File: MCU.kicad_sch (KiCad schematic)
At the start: 46 parts, among them J1 USB_C_Receptacle_USB2.0_16P, J2 DE9_Pins_MountingHoles, Q1 BC817, Q2 BC817, Q3 BC817, Q4 BC817, SW1 SW_SPST, SW2 SW_SPST, U1 W25Q128JVS, U2 ESP32-S3-MINI-1U, U3 MAX3232

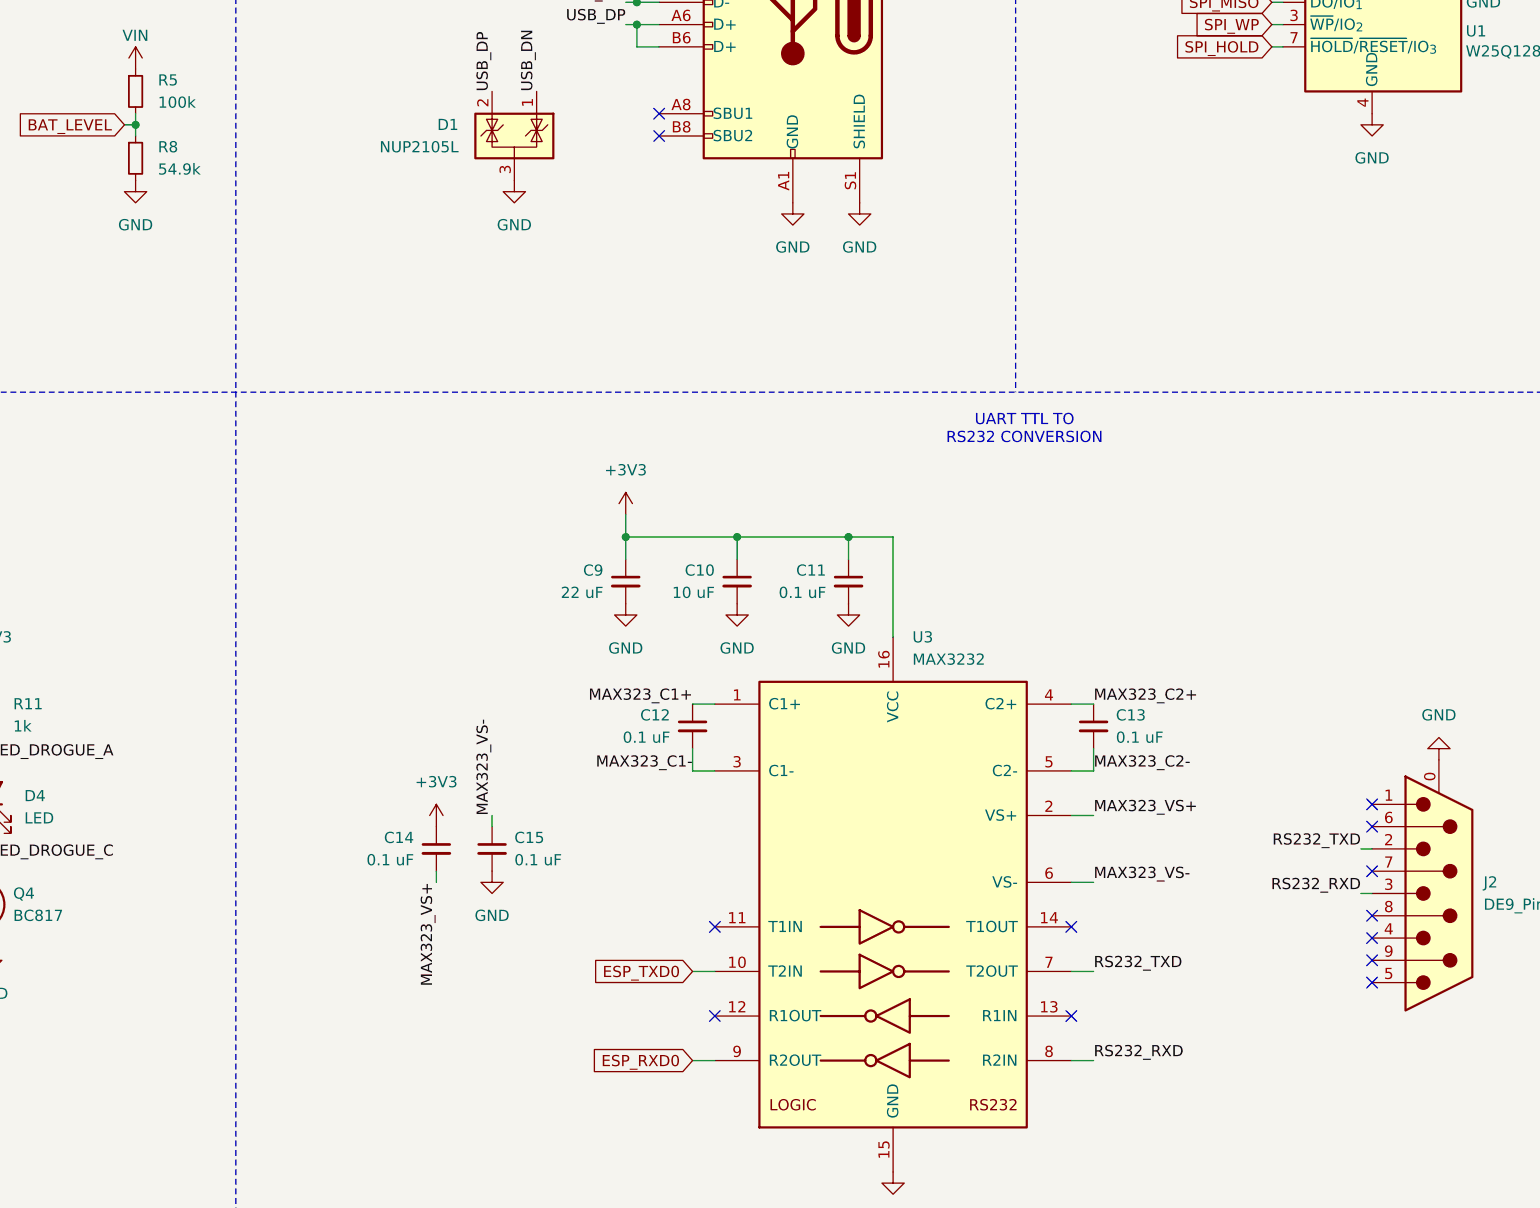
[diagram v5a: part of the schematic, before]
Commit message: updated some values and routed some preliminary roads
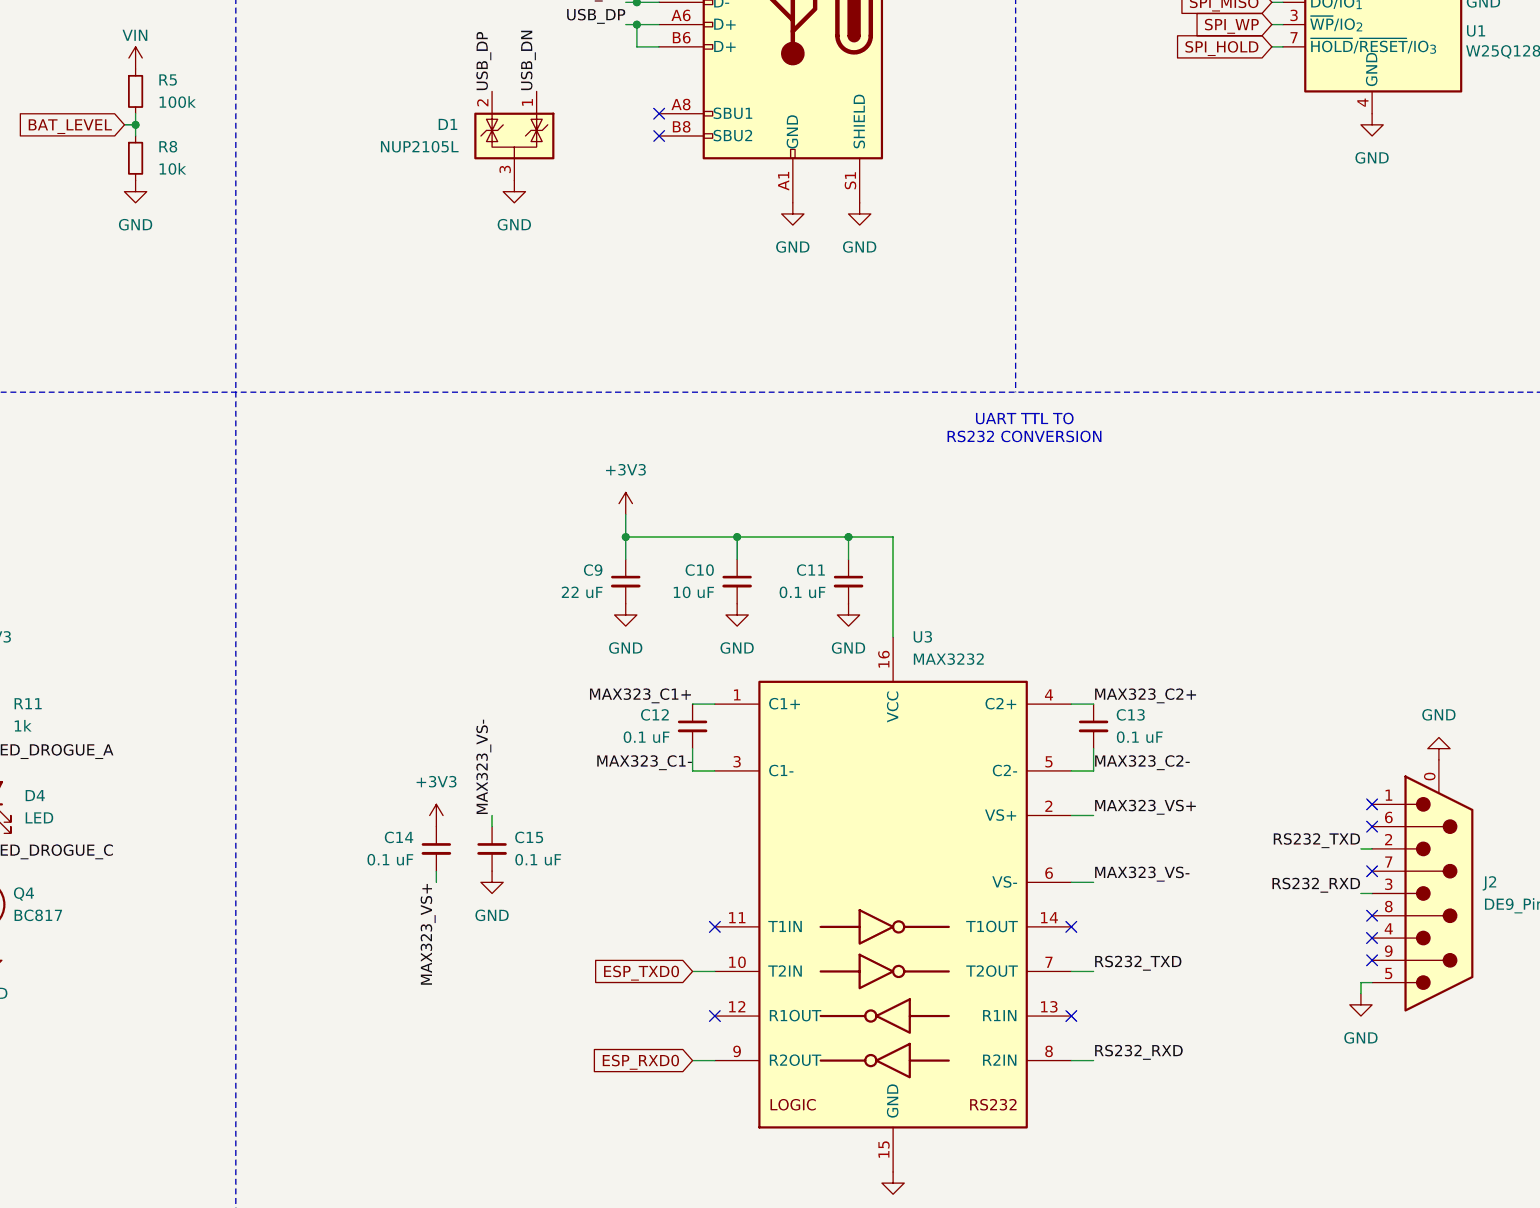
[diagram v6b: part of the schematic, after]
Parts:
- R8: value 54.9k -> 10k
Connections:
- net GND: now also J2.5
- no-connect marks 23 -> 22
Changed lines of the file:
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@@
 	)
 	(no_connect
-		(at 322.58 175.26)
-	)
-	(no_connect
 		(at 102.87 55.88)
 	)
@@
 	(wire
 		(pts
+			(xy 322.58 175.26) (xy 321.31 175.26)
+		)
+		(stroke
+			(width 0)
+			(type default)
+		)
+	)
+	(wire
+		(pts
 			(xy 347.98 57.15) (xy 347.98 58.42)
 		)
@@
 	(wire
 		(pts
+			(xy 321.31 175.26) (xy 321.31 176.53)
+		)
+		(stroke
+			(width 0)
+			(type default)
+		)
+	)
+	(wire
+		(pts
 			(xy 288.29 151.13) (xy 290.83 151.13)
 		)
@@
 	)
 	(symbol
+		(lib_id "power:GND")
+		(at 321.31 176.53 0)
+		(unit 1)
+		(exclude_from_sim no)
+		(in_bom yes)
+		(on_board yes)
+		(dnp no)
+		(fields_autoplaced yes)
+		(property "Reference" "#PWR0119"
+			(at 321.31 182.88 0)
+			(effects
+				(font
+					(size 1.27 1.27)
+				)
+				(hide yes)
+			)
+		)
+		(property "Value" "GND"
+			(at 321.31 181.61 0)
+			(effects
+				(font
+					(size 1.27 1.27)
+				)
+			)
+		)
+		(property "Footprint" ""
+			(at 321.31 176.53 0)
+			(effects
+				(font
+					(size 1.27 1.27)
+				)
+				(hide yes)
+			)
+		)
+		(property "Datasheet" ""
+			(at 321.31 176.53 0)
+			(effects
+				(font
+					(size 1.27 1.27)
+				)
+				(hide yes)
+			)
+		)
+		(property "Description" "Power symbol creates a global label with name \"GND\" , ground"
+			(at 321.31 176.53 0)
+			(effects
+				(font
+					(size 1.27 1.27)
+				)
+				(hide yes)
+			)
+		)
+		(pin "1"
+		)
+		(instances
+			(project "valkyriev3"
+				(path "/d24fd15c-a242-4d26-9876-7755ca0d378c/d62cb9a5-57b0-46af-b3af-5759837aeb39"
+					(reference "#PWR0119")
+					(unit 1)
+				)
+			)
+		)
+	)
+	(symbol
 		(lib_id "Device:R_Small")
 		(at 165.1 144.78 180)
@@
 			)
 		)
-		(property "Value" "54.9k"
+		(property "Value" "10k"
 			(at 184.15 82.5499 0)
 			(effects

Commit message: did some clean-up, did some to-do tasks.
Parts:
- added D1: S2A, Diode_SMD:D_SMB, symbol Device:D_Small
- renumbered D1 to D2, D2 to D3, D3 to D4, D4 to D5
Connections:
- net +5V: now also D1.1 (K); no longer J1.A4 (VBUS), J1.A9 (VBUS), J1.B4 (VBUS), J1.B9 (VBUS)
- net ESP_RXD2: now also U2.36 (IO40); no longer U2.37 (IO41)
- net ESP_TXD2: now also U2.37 (IO41); no longer U2.36 (IO40)
- net LORA_M0: now also U2.20 (IO16); no longer U2.19 (IO15)
- net LORA_M1: now also U2.19 (IO15); no longer U2.20 (IO16)
- new net USB_VBUS: D1.2 (A), J1.A4 (VBUS), J1.A9 (VBUS), J1.B4 (VBUS), J1.B9 (VBUS)

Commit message: improvements, re-did some tasks. updated step file.
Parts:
- removed D1: S2A, Diode_SMD:D_SMB, symbol Device:D_Small
- added D1: 1N4007, Diode_THT:D_DO-41_SOD81_P2.54mm_Vertical_AnodeUp, symbol Diode:1N4007
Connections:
- net +5V: now also D1.1 (K)
- net USB_VBUS: now also D1.2 (A)
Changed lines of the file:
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@@
 	(wire
 		(pts
-			(xy 238.76 38.1) (xy 238.76 40.64)
+			(xy 238.76 38.1) (xy 238.76 39.37)
 		)
 		(stroke
@@
 	(wire
 		(pts
+			(xy 238.76 48.26) (xy 241.3 48.26)
+		)
+		(stroke
+			(width 0)
+			(type default)
+		)
+	)
+	(wire
+		(pts
 			(xy 38.1 68.58) (xy 39.37 68.58)
 		)
@@
 	(wire
 		(pts
-			(xy 238.76 45.72) (xy 238.76 48.26)
-		)
-		(stroke
-			(width 0)
-			(type default)
-		)
-	)
-	(wire
-		(pts
 			(xy 39.37 81.28) (xy 40.64 81.28)
 		)
@@
 	(wire
 		(pts
-			(xy 238.76 48.26) (xy 241.3 48.26)
-		)
-		(stroke
-			(width 0)
-			(type default)
-		)
-	)
-	(wire
-		(pts
 			(xy 113.03 166.37) (xy 115.57 166.37)
 		)
@@
 	(wire
 		(pts
+			(xy 238.76 48.26) (xy 238.76 46.99)
+		)
+		(stroke
+			(width 0)
+			(type default)
+		)
+	)
+	(wire
+		(pts
 			(xy 96.52 161.29) (xy 96.52 157.48)
 		)
@@
 	)
 	(symbol
-		(lib_id "Device:D_Small")
-		(at 238.76 43.18 270)
-		(unit 1)
-		(exclude_from_sim no)
-		(in_bom yes)
-		(on_board yes)
-		(dnp no)
-		(property "Reference" "D1"
-			(at 236.22 44.4501 90)
-			(effects
-				(font
-					(size 1.27 1.27)
-				)
-				(justify right)
-			)
-		)
-		(property "Value" "S2A"
-			(at 236.22 41.9101 90)
-			(effects
-				(font
-					(size 1.27 1.27)
-				)
-				(justify right)
-			)
-		)
-		(property "Footprint" "Diode_SMD:D_SMB"
-			(at 238.76 43.18 90)
-			(effects
-				(font
-					(size 1.27 1.27)
-				)
-				(hide yes)
-			)
-		)
-		(property "Datasheet" "https://www.onsemi.com/pdf/datasheet/s2m-d.pdf"
-			(at 238.76 43.18 90)
-			(effects
-				(font
-					(size 1.27 1.27)
-				)
-				(hide yes)
-			)
-		)
-		(property "Description" "Diode, small symbol"
-			(at 238.76 43.18 0)
-			(effects
-				(font
-					(size 1.27 1.27)
-				)
-				(hide yes)
-			)
-		)
-		(property "Sim.Device" "D"
-			(at 238.76 43.18 0)
-			(effects
-				(font
-					(size 1.27 1.27)
-				)
-				(hide yes)
-			)
-		)
-		(property "Sim.Pins" "1=K 2=A"
-			(at 238.76 43.18 0)
-			(effects
-				(font
-					(size 1.27 1.27)
-				)
-				(hide yes)
-			)
-		)
-		(pin "2"
-		)
-		(pin "1"
-		)
-		(instances
-			(project "valkyriev3"
-				(path "/d24fd15c-a242-4d26-9876-7755ca0d378c/d62cb9a5-57b0-46af-b3af-5759837aeb39"
-					(reference "D1")
-					(unit 1)
-				)
-			)
-		)
-	)
-	(symbol
 		(lib_id "power:GND")
 		(at 321.31 176.53 0)
@@
 					(unit 1)
 				)
+			)
+		)
+	)
+	(symbol
+		(lib_id "Diode:1N4007")
+		(at 238.76 43.18 270)
+		(unit 1)
+		(exclude_from_sim no)
+		(in_bom yes)
+		(on_board yes)
+		(dnp no)
+		(property "Reference" "D1"
+			(at 236.22 41.9099 90)
+			(effects
+				(font
+					(size 1.27 1.27)
+				)
+				(justify right)
+			)
+		)
+		(property "Value" "1N4007"
+			(at 236.22 44.4499 90)
+			(effects
+				(font
+					(size 1.27 1.27)
+				)
+				(justify right)
+			)
+		)
+		(property "Footprint" "Diode_THT:D_DO-41_SOD81_P2.54mm_Vertical_AnodeUp"
+			(at 234.315 43.18 0)
+			(effects
+				(font
+					(size 1.27 1.27)
+				)
+				(hide yes)
+			)
+		)
+		(property "Datasheet" "http://www.vishay.com/docs/88503/1n4001.pdf"
+			(at 238.76 43.18 0)
+			(effects
+				(font
+					(size 1.27 1.27)
+				)
+				(hide yes)
+			)
+		)
+		(property "Description" "1000V 1A General Purpose Rectifier Diode, DO-41"
+			(at 238.76 43.18 0)
+			(effects
+				(font
+					(size 1.27 1.27)
+				)
+				(hide yes)
+			)
+		)
+		(property "Sim.Device" "D"
+			(at 238.76 43.18 0)
+			(effects
+				(font
+					(size 1.27 1.27)
+				)
+				(hide yes)
+			)
+		)
+		(property "Sim.Pins" "1=K 2=A"
+			(at 238.76 43.18 0)
+			(effects
+				(font
+					(size 1.27 1.27)
+				)
+				(hide yes)
+			)
+		)
+		(pin "2"
+		)
+		(pin "1"
+		)
+		(instances
+			(project ""
+				(path "/d24fd15c-a242-4d26-9876-7755ca0d378c/d62cb9a5-57b0-46af-b3af-5759837aeb39"
+					(reference "D1")
+					(unit 1)
+				)
